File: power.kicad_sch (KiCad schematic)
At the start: 16 parts, among them J2 USB_C_Receptacle_USB2.0_16P, J3 Conn_01x02_Pin, U4 USBLC6-2SC6, U5 BQ24090DGQ, U6 MAX17048G, U7 TPS7A0508PDBZ

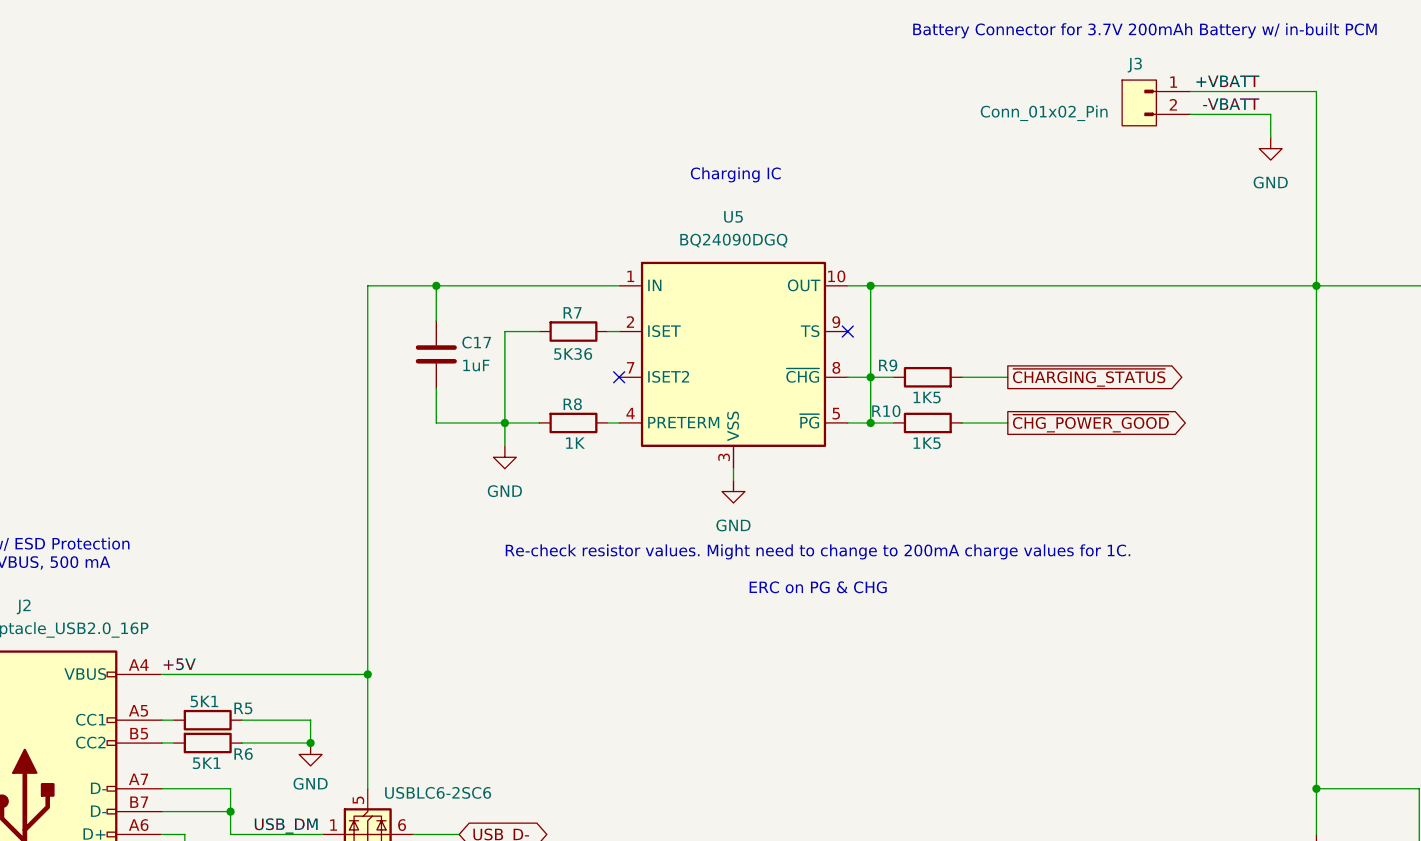
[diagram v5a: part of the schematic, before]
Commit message: Cleaned up local vs. global net labels
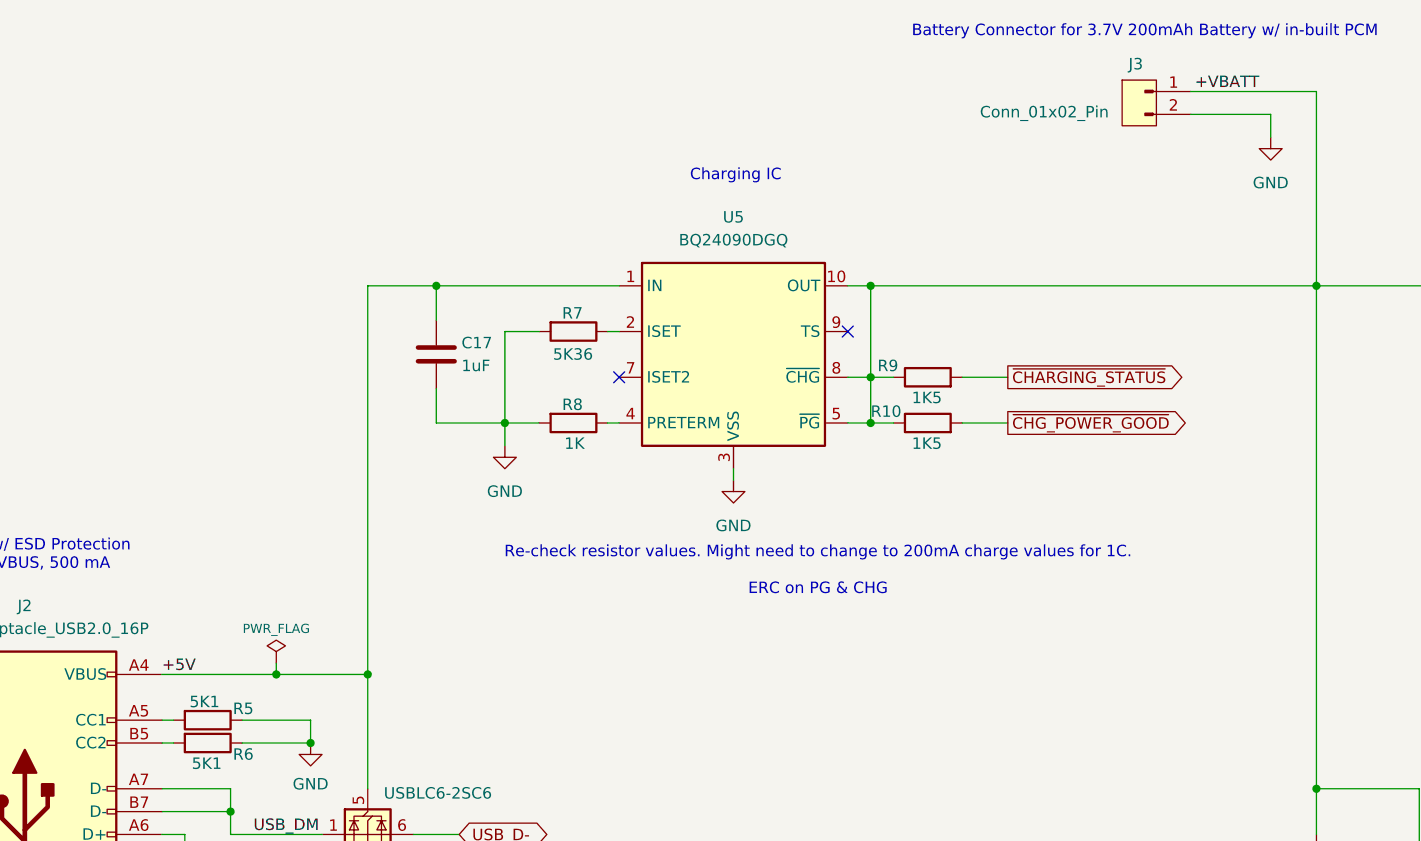
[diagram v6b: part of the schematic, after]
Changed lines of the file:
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@@
+		(color 0 0 0 0)
+	)
+	(junction
+		(at 63.5 99.06)
+		(diameter 0)
 		(color 0 0 0 0)
 	)
@@
 	(wire
 		(pts
+			(xy 63.5 97.79) (xy 63.5 99.06)
+		)
+		(stroke
+			(width 0)
+			(type default)
+		)
+	)
+	(wire
+		(pts
 			(xy 81.28 55.88) (xy 101.6 55.88)
 		)
@@
 	(wire
 		(pts
-			(xy 50.8 99.06) (xy 73.66 99.06)
+			(xy 50.8 99.06) (xy 63.5 99.06)
 		)
 		(stroke
@@
 		(pts
 			(xy 67.31 104.14) (xy 59.69 104.14)
+		)
+		(stroke
+			(width 0)
+			(type default)
+		)
+	)
+	(wire
+		(pts
+			(xy 63.5 99.06) (xy 73.66 99.06)
 		)
 		(stroke
@@
 			)
 			(justify left bottom)
-		)
-	)
-	(label "-VBATT"
-		(at 172.72 36.83 180)
-		(effects
-			(font
-				(size 1.27 1.27)
-			)
-			(justify right bottom)
 		)
 	)
@@
 					(unit 1)
 				)
+			)
+		)
+	)
+	(symbol
+		(lib_id "power:PWR_FLAG")
+		(at 63.5 97.79 0)
+		(unit 1)
+		(exclude_from_sim no)
+		(in_bom yes)
+		(on_board yes)
+		(dnp no)
+		(property "Reference" "#FLG01"
+			(at 63.5 95.885 0)
+			(effects
+				(font
+					(size 1.27 1.27)
+				)
+				(hide yes)
+			)
+		)
+		(property "Value" "PWR_FLAG"
+			(at 63.5 93.98 0)
+			(effects
+				(font
+					(size 1.016 1.016)
+				)
+			)
+		)
+		(property "Footprint" ""
+			(at 63.5 97.79 0)
+			(effects
+				(font
+					(size 1.27 1.27)
+				)
+				(hide yes)
+			)
+		)
+		(property "Datasheet" "~"
+			(at 63.5 97.79 0)
+			(effects
+				(font
+					(size 1.27 1.27)
+				)
+				(hide yes)
+			)
+		)
+		(property "Description" "Special symbol for telling ERC where power comes from"
+			(at 63.5 97.79 0)
+			(effects
+				(font
+					(size 1.27 1.27)
+				)
+				(hide yes)
+			)
+		)
+		(pin "1"
+		)
+		(instances
+			(project ""
+				(path "/29eb74dc-e91c-4cc5-ad9f-7f8caf36d690/50aa898a-4cd9-4f6c-a569-964480767df5"
+					(reference "#FLG01")
+					(unit 1)
+				)

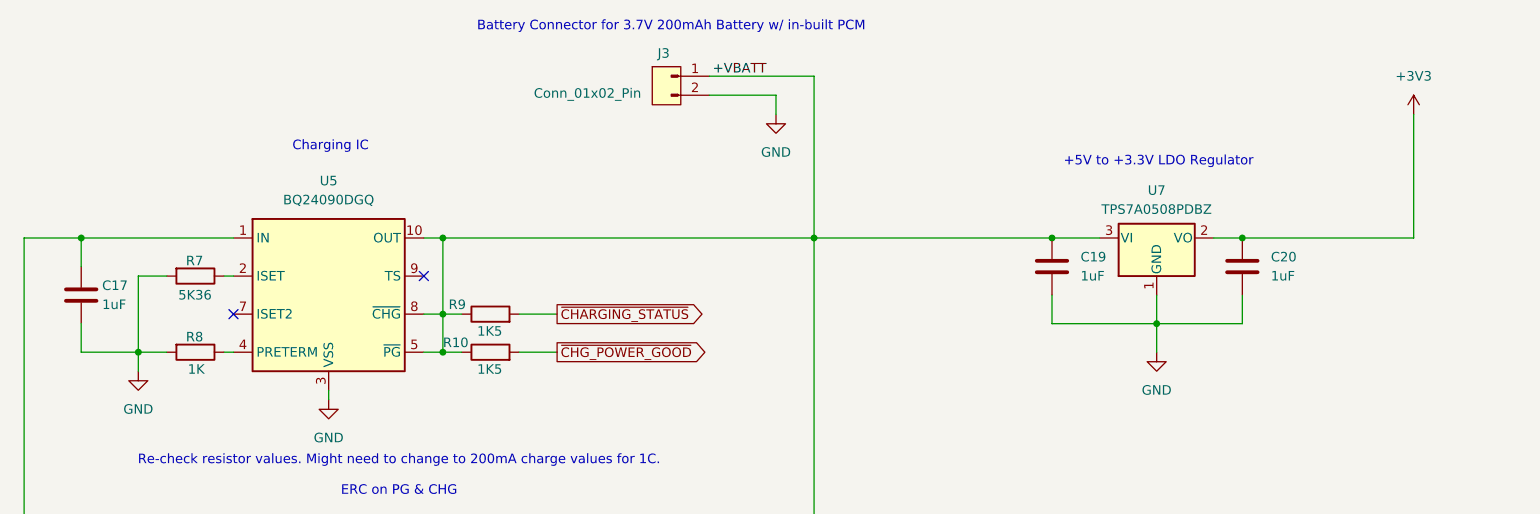
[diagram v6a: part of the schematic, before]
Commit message: ERC Check fixes
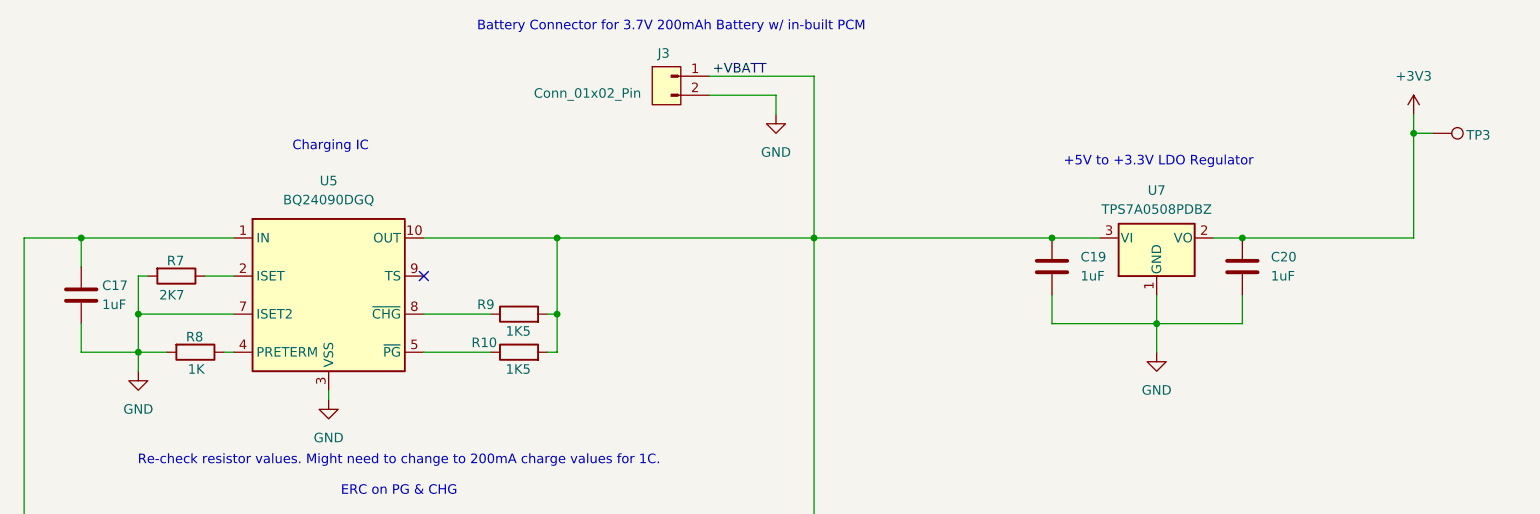
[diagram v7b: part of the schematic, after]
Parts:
- added TP3: ~, symbol Connector:TestPoint
- R7: value 5K36 -> 2K7
- U5: footprint Package_SO:HVSSOP-10-1EP_3x3mm_P0.5mm_EP1.57x1.88mm_ThermalVias -> LibraryFootprints:MLPF-WB55-01E3
- U6: footprint MAX17048G_:SON50P200X200X80-9N -> LibraryFootprints:SON50P200X200X80-9N
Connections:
- net ~{CHARGING_STATUS} is gone; now on net +VBATT: R9.2
- net ~{CHG_POWER_GOOD} is gone; now on net +VBATT: R10.2
- net +3V3: now also TP3.1
- net +VBATT: no longer R10.1, R9.1, U5.5 (~{PG}), U5.8 (~{CHG})
- net GND: now also U5.7 (ISET2)
- new net: R10.1, U5.5 (~{PG})
- new net: R9.1, U5.8 (~{CHG})
- no-connect marks 4 -> 3
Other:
- moved on the sheet: R10, R7, R9

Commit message: Added test points and other cleanup
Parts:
- added TP4: ~, TestPoint:TestPoint_Pad_D1.0mm, symbol Connector:TestPoint
- J2: footprint (none) -> Connector_USB:USB_C_Receptacle_Molex_105450-0101; Digikey Link (none) -> https://www.digikey.com/en/products/detail/molex/1054500101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; MPN (none) -> 1054500101
- TP3: footprint (none) -> TestPoint:TestPoint_Pad_D1.0mm
- U6: footprint LibraryFootprints:SON50P200X200X80-9N -> Package_DFN_QFN:TDFN-8-1EP_2x2mm_P0.5mm_EP0.8x1.2mm
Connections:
- net GND: now also TP4.1
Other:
- note added: "Ground Test Point"
- note removed: "Re-check resistor values. Might need to change to 200mA charge values for 1C. ERC on PG & CHG"
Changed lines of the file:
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@@
 	(text "Fuel Gauge IC"
 		(exclude_from_sim no)
-		(at 216.662 98.806 0)
+		(at 215.9 96.012 0)
 		(effects
 			(font
-				(size 1.27 1.27)
+				(size 2.032 2.032)
 			)
 		)
 	)
-	(text "Re-check resistor values. Might need to change to 200mA charge values for 1C. \n\nERC on PG & CHG"
+	(text "Charging IC"
 		(exclude_from_sim no)
-		(at 123.698 87.63 0)
+		(at 114.554 43.688 0)
 		(effects
 			(font
-				(size 1.27 1.27)
+				(size 2.032 2.032)
 			)
 		)
 	)
-	(text "Charging IC"
+	(text "Ground Test Point"
 		(exclude_from_sim no)
-		(at 114.554 43.688 0)
+		(at 136.398 157.988 0)
 		(effects
 			(font
-				(size 1.27 1.27)
+				(size 2.032 2.032)
 			)
 		)
@@
 		(effects
 			(font
-				(size 1.27 1.27)
+				(size 2.032 2.032)
 			)
 		)
 	)
-	(text "Battery Connector for 3.7V 200mAh Battery w/ in-built PCM"
+	(text "Battery Connector for 3.7V 200mAh Battery\nw/ in-built PCM"
 		(exclude_from_sim no)
-		(at 160.02 27.686 0)
+		(at 159.766 23.876 0)
 		(effects
 			(font
-				(size 1.27 1.27)
+				(size 2.032 2.032)
 			)
 		)
@@
 		(effects
 			(font
-				(size 1.27 1.27)
+				(size 2.032 2.032)
 			)
 		)
@@
 	(wire
 		(pts
+			(xy 137.16 168.91) (xy 137.16 171.45)
+		)
+		(stroke
+			(width 0)
+			(type default)
+		)
+	)
+	(wire
+		(pts
 			(xy 179.07 124.46) (xy 179.07 130.81)
 		)
@@
 			)
 		)
-		(property "Footprint" ""
+		(property "Footprint" "Connector_USB:USB_C_Receptacle_Molex_105450-0101"
 			(at 39.37 114.3 0)
 			(effects
@@
 			)
 		)
+		(property "MPN" "1054500101"
+			(at 35.56 114.3 0)
+			(effects
+				(font
+					(size 1.27 1.27)
+				)
+				(hide yes)
+			)
+		)
+		(property "Digikey Link" "https://www.digikey.com/en/products/detail/molex/1054500101/5843890"
+			(at 35.56 114.3 0)
+			(effects
+				(font
+					(size 1.27 1.27)
+				)
+				(hide yes)
+			)
+		)
 		(pin "A1"
 		)
@@
 	)
 	(symbol
+		(lib_id "Connector:TestPoint")
+		(at 137.16 168.91 0)
+		(unit 1)
+		(exclude_from_sim no)
+		(in_bom yes)
+		(on_board yes)
+		(dnp no)
+		(property "Reference" "TP4"
+			(at 137.414 162.814 0)
+			(effects
+				(font
+					(size 1.27 1.27)
+				)
+			)
+		)
+		(property "Value" "~"
+			(at 136.652 166.878 90)
+			(effects
+				(font
+					(size 1.27 1.27)
+				)
+				(hide yes)
+			)
+		)
+		(property "Footprint" "TestPoint:TestPoint_Pad_D1.0mm"
+			(at 142.24 168.91 0)
+			(effects
+				(font
+					(size 1.27 1.27)
+				)
+				(hide yes)
+			)
+		)
+		(property "Datasheet" "~"
+			(at 142.24 168.91 0)
+			(effects
+				(font
+					(size 1.27 1.27)
+				)
+				(hide yes)
+			)
+		)
+		(property "Description" "test point"
+			(at 137.16 168.91 0)
+			(effects
+				(font
+					(size 1.27 1.27)
+				)
+				(hide yes)
+			)
+		)
+		(pin "1"
+		)
+		(instances
+			(project "2tonewatch"
+				(path "/29eb74dc-e91c-4cc5-ad9f-7f8caf36d690/50aa898a-4cd9-4f6c-a569-964480767df5"
+					(reference "TP4")
+					(unit 1)
+				)
+			)
+		)
+	)
+	(symbol
 		(lib_id "Power_Protection:USBLC6-2SC6")
 		(at 73.66 116.84 0)
@@
 			)
 		)
-		(property "Footprint" ""
+		(property "Footprint" "TestPoint:TestPoint_Pad_D1.0mm"
 			(at 261.62 46.99 0)
 			(effects
@@
 			)
 		)
-		(property "Footprint" "LibraryFootprints:SON50P200X200X80-9N"
+		(property "Footprint" "Package_DFN_QFN:TDFN-8-1EP_2x2mm_P0.5mm_EP0.8x1.2mm"
 			(at 215.9 121.92 0)
 			(effects
@@
 					(size 1.016 1.016)
 				)
+				(hide yes)
 			)
 		)
@@
 					(unit 1)
 				)
+			)
+		)
+	)
+	(symbol
+		(lib_id "power:GND")
+		(at 137.16 171.45 0)
+		(unit 1)
+		(exclude_from_sim no)
+		(in_bom yes)
+		(on_board yes)
+		(dnp no)
+		(fields_autoplaced yes)
+		(property "Reference" "#PWR08"
+			(at 137.16 177.8 0)
+			(effects
+				(font
+					(size 1.27 1.27)
+				)
+				(hide yes)
+			)
+		)
+		(property "Value" "GND"
+			(at 137.16 176.53 0)
+			(effects
+				(font
+					(size 1.27 1.27)
+				)
+			)
+		)
+		(property "Footprint" ""
+			(at 137.16 171.45 0)
+			(effects
+				(font
+					(size 1.27 1.27)
+				)
+				(hide yes)
+			)
+		)
+		(property "Datasheet" ""
+			(at 137.16 171.45 0)
+			(effects
+				(font
+					(size 1.27 1.27)
+				)
+				(hide yes)
+			)
+		)
+		(property "Description" "Power symbol creates a global label with name \"GND\" , ground"
+			(at 137.16 171.45 0)
+			(effects
+				(font
+					(size 1.27 1.27)
+				)
+				(hide yes)
+			)
+		)
+		(pin "1"
+		)
+		(instances
+			(project "2tonewatch"
+				(path "/29eb74dc-e91c-4cc5-ad9f-7f8caf36d690/50aa898a-4cd9-4f6c-a569-964480767df5"
+					(reference "#PWR08")
+					(unit 1)
+				)
